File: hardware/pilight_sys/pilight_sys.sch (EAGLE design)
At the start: 23 parts, among them IC1 TINY13-20PU, IC2 74ABT125DB, P1 B2P-VH, P2 B2P-VH, P3 B4B-PH-K, P4 B2B-PH-K, P5 B2B-PH-K, P6 B2P-VH, P7 B2B-PH-K, Q1 IRLB8748PBF-VER

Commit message: Finished v1 eagle designs
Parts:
- P3: value B4B-PH-K -> B2P-VH; device con-jst-ph:B4B-PH-K -> con-jst-vh:B2P-VH
- P6: value B2P-VH -> B2B-PH-K; device con-jst-vh:B2P-VH -> con-jst-ph:B2B-PH-K
- P7: value B2B-PH-K -> B4B-PH-K; device con-jst-ph:B2B-PH-K -> con-jst-ph:B4B-PH-K
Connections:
- net GND: now also P7.1; no longer P3.1
- net N$1: now also P4.1; no longer P7.1
- net N$13: now also P7.2; no longer P3.2
- net N$2: now also P4.2; no longer P7.2
- net N$5: now also P3.2; no longer P6.2
- net N$6: now also P6.1; no longer P4.1
- net N$7: now also P6.2; no longer P4.2
- net N$8: now also P7.3; no longer P3.3
- net VCC: now also P3.1, P7.4; no longer P3.4, P6.1
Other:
- moved on the sheet: P4, P6
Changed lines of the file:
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@@
 <part name="P1" library="con-jst-vh" deviceset="B2P-VH" device=""/>
 <part name="P2" library="con-jst-vh" deviceset="B2P-VH" device=""/>
-<part name="P3" library="con-jst-ph" deviceset="B4B-PH-K" device=""/>
+<part name="P7" library="con-jst-ph" deviceset="B4B-PH-K" device=""/>
+<part name="P6" library="con-jst-ph" deviceset="B2B-PH-K" device=""/>
+<part name="P5" library="con-jst-ph" deviceset="B2B-PH-K" device=""/>
 <part name="P4" library="con-jst-ph" deviceset="B2B-PH-K" device=""/>
-<part name="P5" library="con-jst-ph" deviceset="B2B-PH-K" device=""/>
-<part name="P7" library="con-jst-ph" deviceset="B2B-PH-K" device=""/>
 <part name="P+1" library="supply1" library_urn="urn:adsk.eagle:library:371" deviceset="VCC" device=""/>
 <part name="P+2" library="supply1" library_urn="urn:adsk.eagle:library:371" deviceset="VCC" device=""/>
@@
 <part name="P+3" library="supply1" library_urn="urn:adsk.eagle:library:371" deviceset="VCC" device=""/>
 <part name="P+4" library="supply1" library_urn="urn:adsk.eagle:library:371" deviceset="VCC" device=""/>
-<part name="P6" library="con-jst-vh" deviceset="B2P-VH" device=""/>
+<part name="P3" library="con-jst-vh" deviceset="B2P-VH" device=""/>
 <part name="P+5" library="supply1" library_urn="urn:adsk.eagle:library:371" deviceset="VCC" device=""/>
 <part name="Q1" library="my_library" deviceset="IRLB8748PBF-VER" device=""/>
@@
 <instance part="P1" gate="G$1" x="203.2" y="144.78"/>
 <instance part="P2" gate="G$1" x="203.2" y="104.14"/>
-<instance part="P3" gate="G$1" x="58.42" y="58.42" rot="R270"/>
-<instance part="P4" gate="G$1" x="86.36" y="58.42" rot="R270"/>
+<instance part="P7" gate="G$1" x="58.42" y="58.42" rot="R270"/>
+<instance part="P6" gate="G$1" x="86.36" y="58.42" rot="R270"/>
 <instance part="P5" gate="G$1" x="203.2" y="71.12"/>
-<instance part="P7" gate="G$1" x="149.86" y="43.18" rot="R270"/>
+<instance part="P4" gate="G$1" x="149.86" y="43.18" rot="R270"/>
 <instance part="P+1" gate="VCC" x="157.48" y="71.12" rot="R90"/>
 <instance part="P+2" gate="VCC" x="157.48" y="50.8" rot="R90"/>
@@
 <instance part="P+3" gate="VCC" x="193.04" y="144.78" rot="R90"/>
 <instance part="P+4" gate="VCC" x="195.58" y="109.22"/>
-<instance part="P6" gate="G$1" x="203.2" y="119.38"/>
+<instance part="P3" gate="G$1" x="203.2" y="119.38"/>
 <instance part="P+5" gate="VCC" x="195.58" y="124.46"/>
 <instance part="Q1" gate="G$1" x="167.64" y="119.38" rot="R270"/>
@@
 </segment>
 <segment>
-<pinref part="P6" gate="G$1" pin="1"/>
+<pinref part="P3" gate="G$1" pin="1"/>
 <pinref part="P+5" gate="VCC" pin="VCC"/>
 <wire x1="198.12" y1="119.38" x2="195.58" y2="119.38" width="0.1524" layer="91"/>
@@
 <pinref part="P+6" gate="VCC" pin="VCC"/>
 <wire x1="53.34" y1="66.04" x2="55.88" y2="66.04" width="0.1524" layer="91"/>
-<pinref part="P3" gate="G$1" pin="4"/>
+<pinref part="P7" gate="G$1" pin="4"/>
 <wire x1="55.88" y1="66.04" x2="55.88" y2="63.5" width="0.1524" layer="91"/>
 </segment>
@@
 </segment>
 <segment>
-<pinref part="P3" gate="G$1" pin="1"/>
+<pinref part="P7" gate="G$1" pin="1"/>
 <wire x1="63.5" y1="63.5" x2="63.5" y2="66.04" width="0.1524" layer="91"/>
 <pinref part="GND4" gate="1" pin="GND"/>
@@
 <net name="N$5" class="0">
 <segment>
-<pinref part="P6" gate="G$1" pin="2"/>
+<pinref part="P3" gate="G$1" pin="2"/>
 <pinref part="Q1" gate="G$1" pin="D"/>
 <wire x1="198.12" y1="116.84" x2="185.42" y2="116.84" width="0.1524" layer="91"/>
@@
 <wire x1="88.9" y1="68.58" x2="86.36" y2="68.58" width="0.1524" layer="91"/>
 <wire x1="86.36" y1="68.58" x2="86.36" y2="66.04" width="0.1524" layer="91"/>
-<pinref part="P4" gate="G$1" pin="1"/>
+<pinref part="P6" gate="G$1" pin="1"/>
 <wire x1="86.36" y1="66.04" x2="86.36" y2="63.5" width="0.1524" layer="91"/>
 <pinref part="R1" gate="G$1" pin="1"/>
@@
 <net name="N$7" class="0">
 <segment>
-<pinref part="P4" gate="G$1" pin="2"/>
+<pinref part="P6" gate="G$1" pin="2"/>
 <wire x1="83.82" y1="63.5" x2="83.82" y2="68.58" width="0.1524" layer="91"/>
 <wire x1="83.82" y1="68.58" x2="78.74" y2="68.58" width="0.1524" layer="91"/>
@@
 <net name="N$1" class="0">
 <segment>
-<pinref part="P7" gate="G$1" pin="1"/>
+<pinref part="P4" gate="G$1" pin="1"/>
 <wire x1="149.86" y1="48.26" x2="149.86" y2="63.5" width="0.1524" layer="91"/>
 <wire x1="149.86" y1="63.5" x2="152.4" y2="63.5" width="0.1524" layer="91"/>
@@
 <net name="N$2" class="0">
 <segment>
-<pinref part="P7" gate="G$1" pin="2"/>
+<pinref part="P4" gate="G$1" pin="2"/>
 <wire x1="147.32" y1="48.26" x2="147.32" y2="83.82" width="0.1524" layer="91"/>
 <wire x1="147.32" y1="83.82" x2="149.86" y2="83.82" width="0.1524" layer="91"/>
@@
 <net name="N$8" class="0">
 <segment>
-<pinref part="P3" gate="G$1" pin="3"/>
+<pinref part="P7" gate="G$1" pin="3"/>
 <wire x1="58.42" y1="63.5" x2="58.42" y2="73.66" width="0.1524" layer="91"/>
 <pinref part="R4" gate="G$1" pin="2"/>
@@
 <net name="N$13" class="0">
 <segment>
-<pinref part="P3" gate="G$1" pin="2"/>
+<pinref part="P7" gate="G$1" pin="2"/>
 <pinref part="IC1" gate="G$1" pin="PB2/PCINT2/SCK/ADC1/T0"/>
 <wire x1="60.96" y1="63.5" x2="60.96" y2="101.6" width="0.1524" layer="91"/>

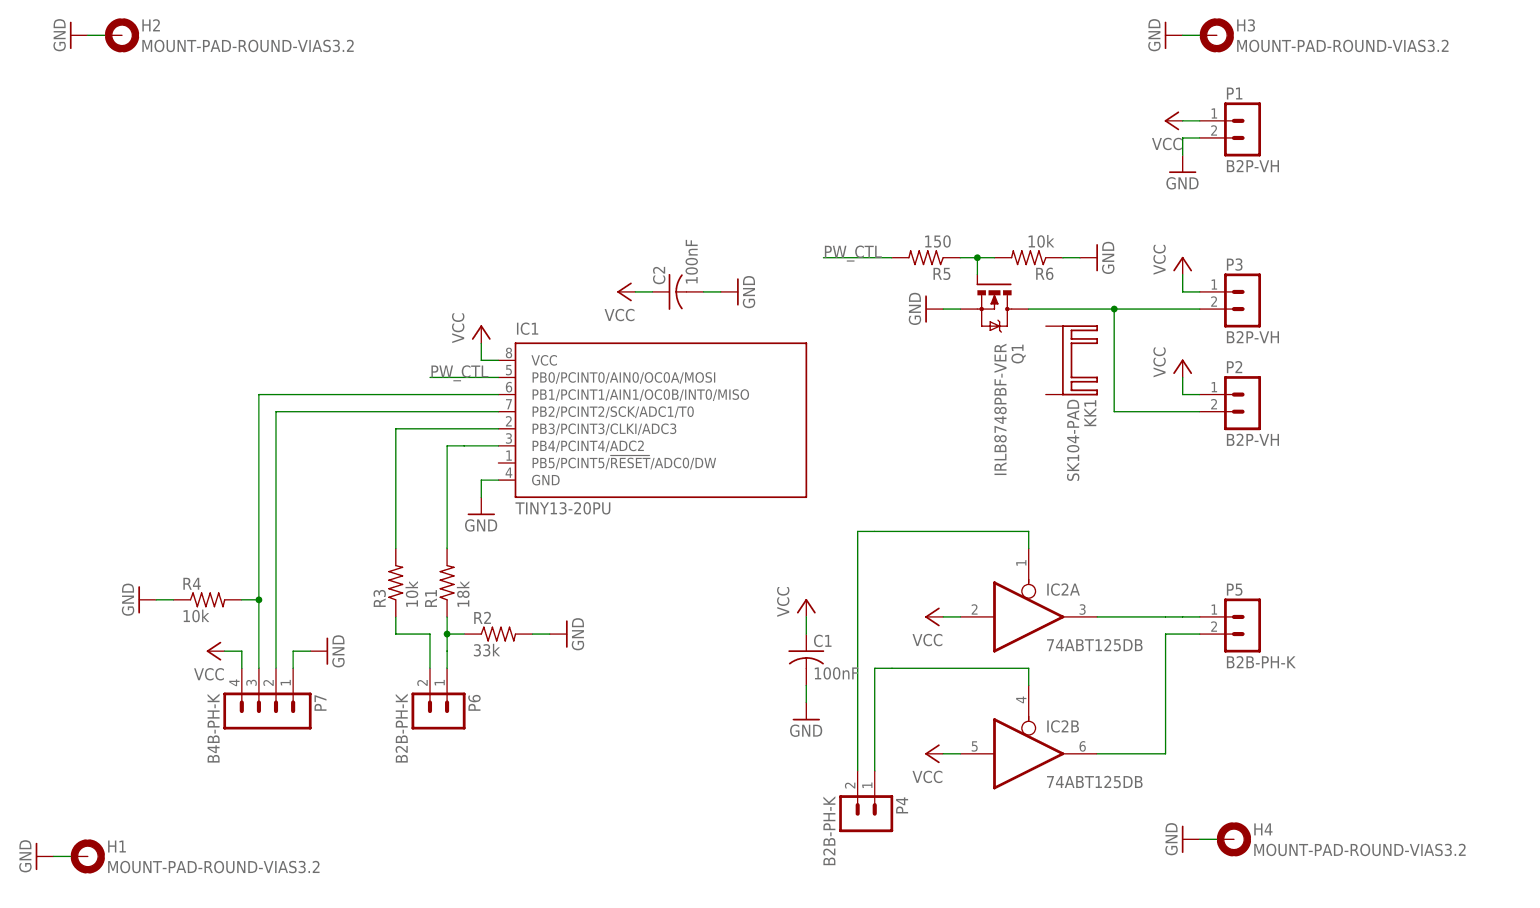
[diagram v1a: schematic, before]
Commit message: Fix bug in circuit (3-state buffer)
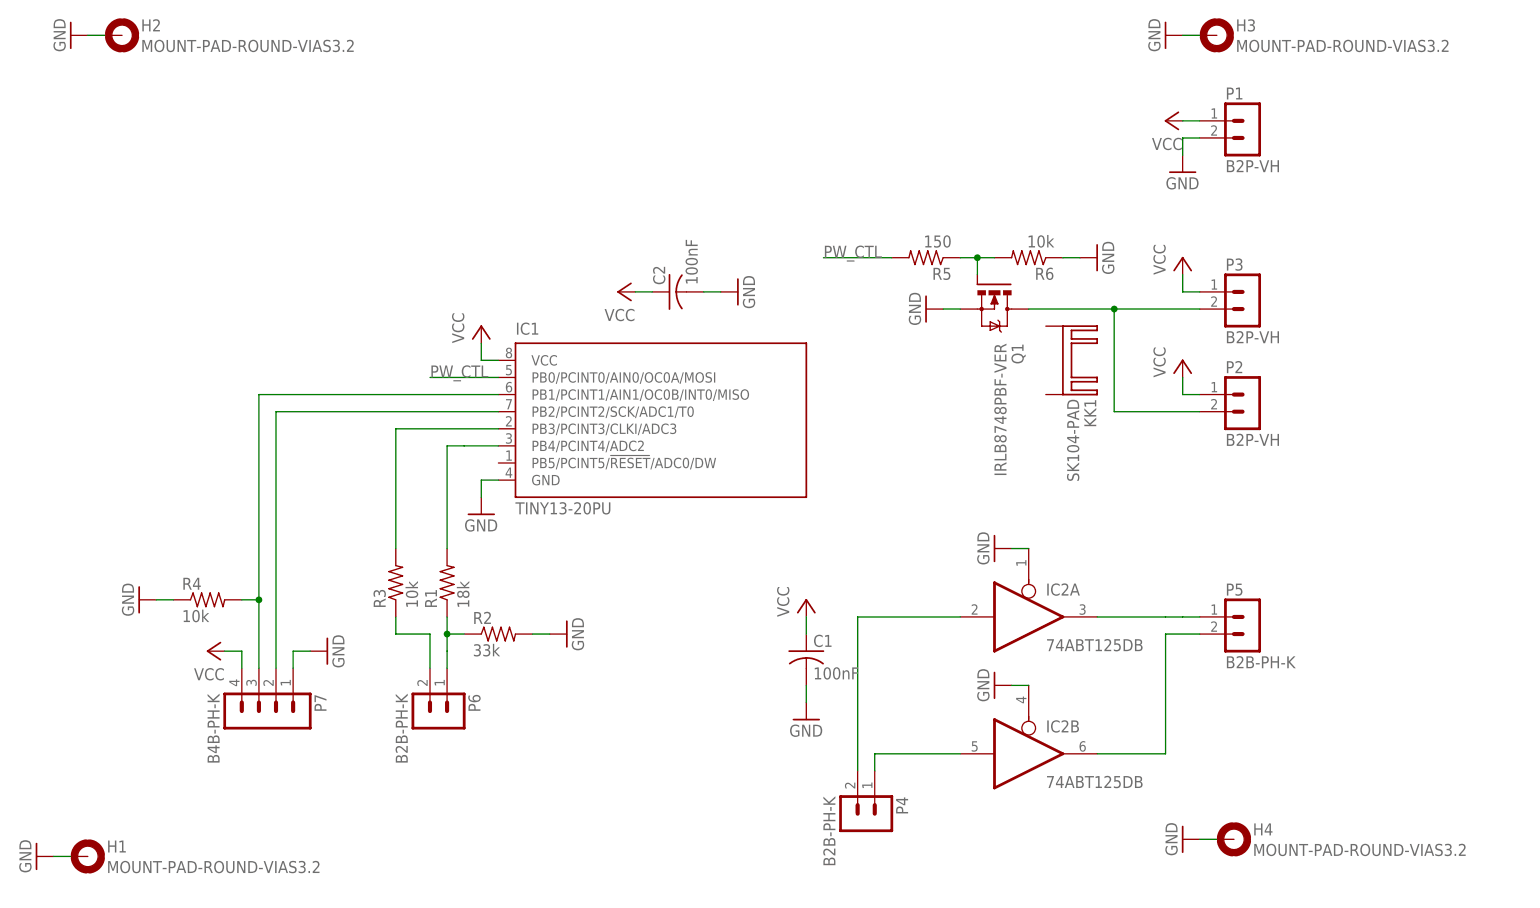
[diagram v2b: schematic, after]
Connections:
- net GND: now also IC2A.OE, IC2B.OE
- net N$1: now also IC2B.I; no longer IC2B.OE
- net N$2: now also IC2A.I; no longer IC2A.OE
- net VCC: no longer IC2A.I, IC2B.I
